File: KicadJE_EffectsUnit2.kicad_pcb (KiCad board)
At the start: 2 copper layers, 100 x 100 mm, 275 parts, among them J201 CV1, J202 CV2, J203 OUT1, J204 OUT2, J205 IN1, J206 IN2, J301 AVR-ISP-6, J302 UART, J401 CV1, J402 CV2, J403 OUT1, J404 OUT2, J405 OUT3, J406 OUT4, J407 IN1, J408 IN2, J409 I2C, J501 BOOT, J502 UART, J503 USB_B_Micro, J601 CV1, J602 FM_lin, J603 Sync, J604 PWM, J605 Ramp, J606 Tri, J608 555_Pulse, P201 Doepfer_Power_16pin, P401 Doepfer_Power_16pin, P601 Doepfer_Power_10pin, Q601 MMBT2222A, SW201 SW_SPDT, SW401 SW_SPDT, U201 TL072, U202 MCP4822, U301 ATmega32A-AU, U401 TL072, U402 TL072, U405 MCP4822, U501 AMS1117-3.3, U502 STM32F103C8Tx, U601 TLC555, U602 TL074, U603 TL074, Y301 16MHz, Y501 8 MHz

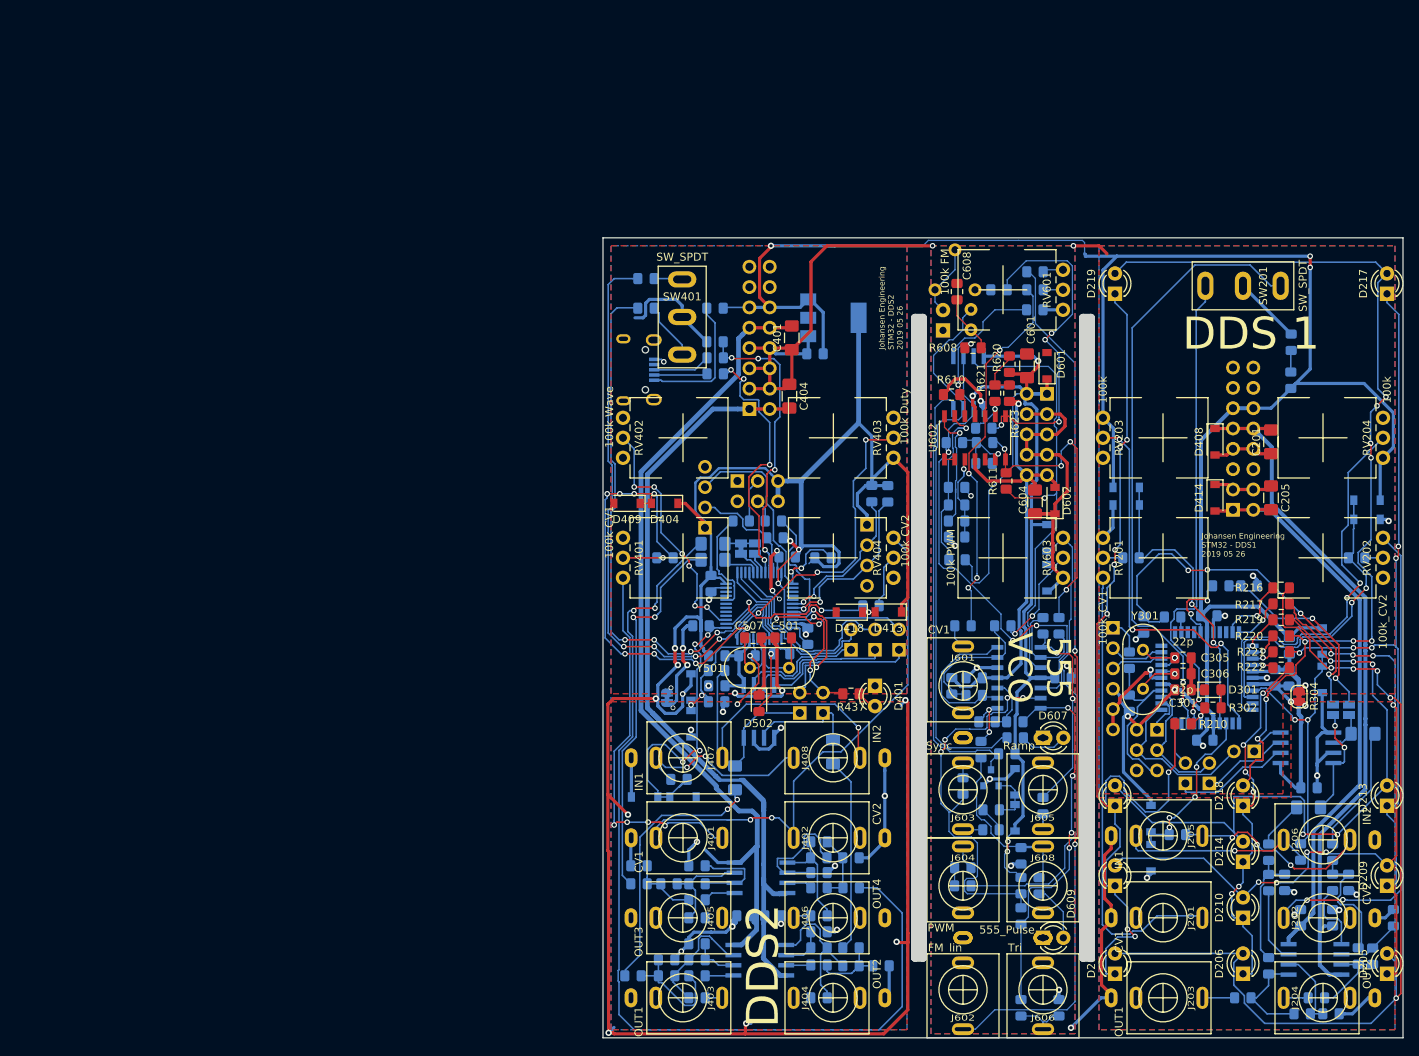
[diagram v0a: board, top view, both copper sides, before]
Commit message: New DPDT footprint
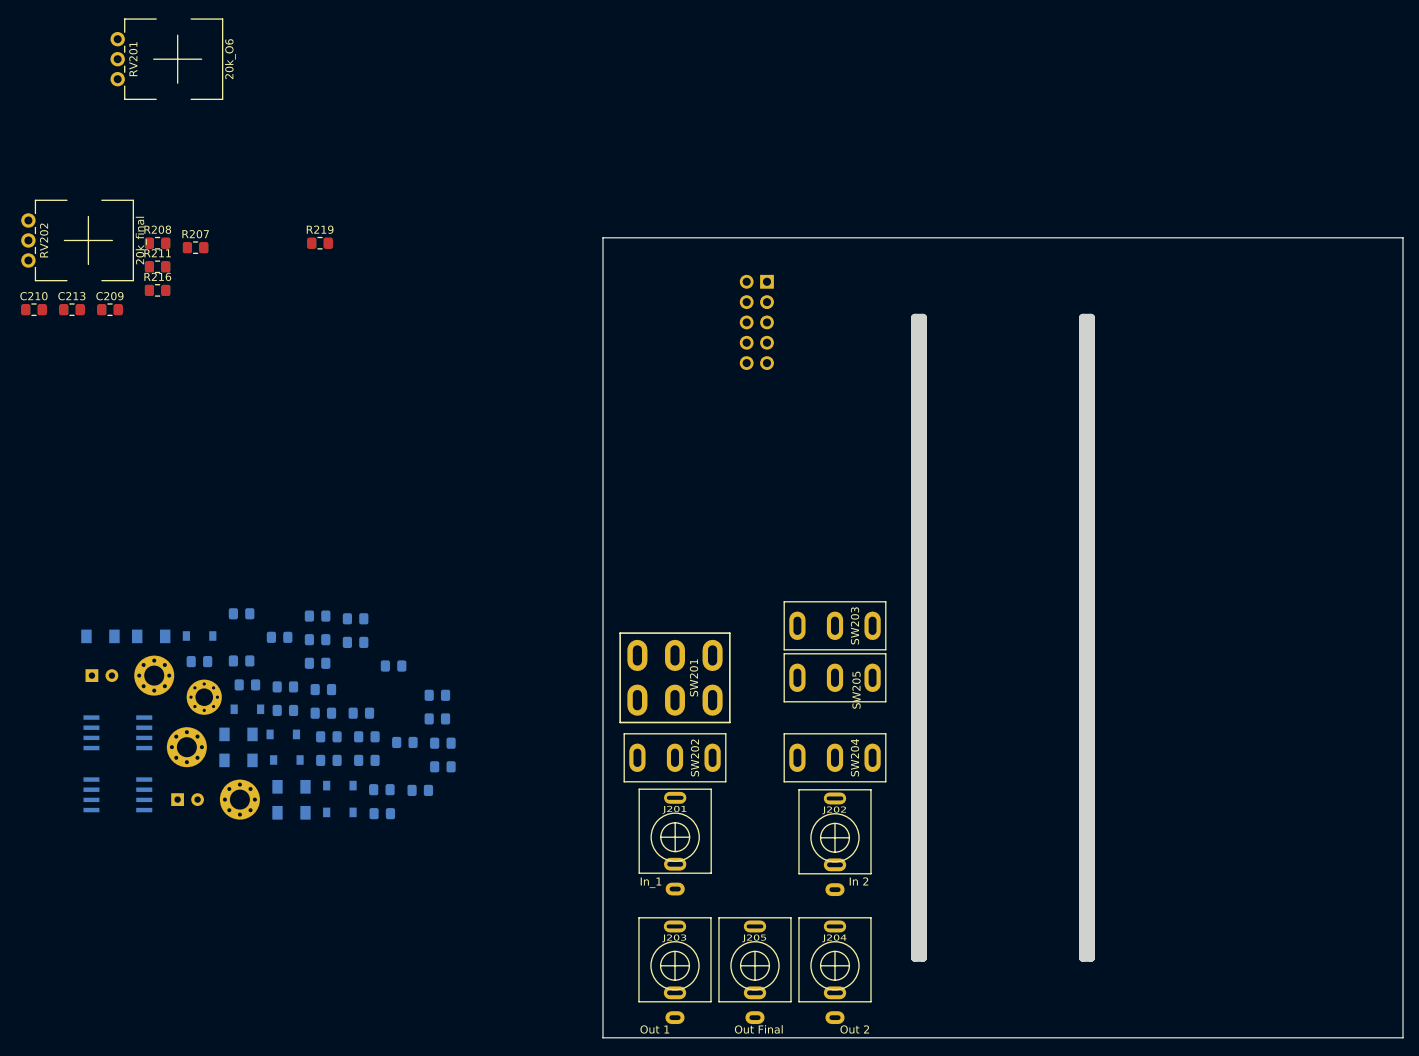
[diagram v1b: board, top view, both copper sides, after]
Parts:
- removed C301, C302, C303, C304, C307, C402, C403, C405, C406, C409, C410, C411, C412, C415, C416, C417, C503, C504, C505, C506, C602, C603, C605: 100n, Capacitor_SMD:C_0805_2012Metric_Pad1.15x1.40mm_HandSolder
- removed C305, C306: 22p, Capacitor_SMD:C_0805_2012Metric_Pad1.15x1.40mm_HandSolder
- removed C401, C404, C407, C408, C413, C414, C601, C604: 1u, Capacitor_SMD:C_1206_3216Metric_Pad1.42x1.75mm_HandSolder
- removed C501, C507: 20p, Capacitor_SMD:C_0805_2012Metric_Pad1.15x1.40mm_HandSolder
- removed C502: 470n, Capacitor_SMD:C_0805_2012Metric_Pad1.15x1.40mm_HandSolder
- removed C606, C610, C611: 1n, Capacitor_SMD:C_0805_2012Metric_Pad1.15x1.40mm_HandSolder
- removed C607: 22n, Capacitor_SMD:C_0805_2012Metric_Pad1.15x1.40mm_HandSolder
- removed C608: 10n, Capacitor_SMD:C_0805_2012Metric_Pad1.15x1.40mm_HandSolder
- removed C609: 220n, Capacitor_SMD:C_0805_2012Metric_Pad1.15x1.40mm_HandSolder
- removed D215, D217, D218, D219, D401, D607, D609: LED, LED_THT:LED_D3.0mm
- removed D216, D220, D404, D408, D409, D413, D414, D418, D419, D420, D421, D422, D601, D602, D603, D604, D605, D606: 1N1007, Diode_SMD:D_SOD-123
- removed D301, D501, D502: LED, LED_SMD:LED_0805_2012Metric_Pad1.15x1.40mm_HandSolder
- removed D611: Vactrol, LED_THT:LED_D3.0mm
- removed J206, J408: IN2, AJ-Dropbox-Kicad:PJ301SM
- removed J301: AVR-ISP-6, Connector_PinHeader_2.54mm:PinHeader_2x03_P2.54mm_Vertical
- removed J302: UART, Connector_PinHeader_2.54mm:PinHeader_1x06_P2.54mm_Vertical
- removed J401, J601: CV1, AJ-Dropbox-Kicad:PJ301SM
- removed J402: CV2, AJ-Dropbox-Kicad:PJ301SM
- removed J403: OUT1, AJ-Dropbox-Kicad:PJ301SM
- removed J404: OUT2, AJ-Dropbox-Kicad:PJ301SM
- removed J405: OUT3, AJ-Dropbox-Kicad:PJ301SM
- removed J406: OUT4, AJ-Dropbox-Kicad:PJ301SM
- removed J407: IN1, AJ-Dropbox-Kicad:PJ301SM
- removed J409: I2C, Connector_PinHeader_2.54mm:PinHeader_1x04_P2.54mm_Vertical
- removed J501: BOOT, Connector_PinHeader_2.54mm:PinHeader_2x03_P2.54mm_Vertical
- removed J502: UART, Connector_PinHeader_2.54mm:PinHeader_1x04_P2.54mm_Vertical
- removed J503: USB_B_Micro, Connector_USB:USB_Micro-B_Wuerth_629105150521
- removed J602: FM_lin, AJ-Dropbox-Kicad:PJ301SM
- removed J603: Sync, AJ-Dropbox-Kicad:PJ301SM
- removed J604: PWM, AJ-Dropbox-Kicad:PJ301SM
- removed J605: Ramp, AJ-Dropbox-Kicad:PJ301SM
- removed J606: Tri, AJ-Dropbox-Kicad:PJ301SM
- removed J608: 555_Pulse, AJ-Dropbox-Kicad:PJ301SM
- removed JP201: SS, Connector_PinSocket_2.54mm:PinSocket_1x02_P2.54mm_Vertical
- removed JP202: MOSI, Connector_PinSocket_2.54mm:PinSocket_1x02_P2.54mm_Vertical
- removed JP203: PWM1, Jumper:SolderJumper-2_P1.3mm_Open_Pad1.0x1.5mm
- removed JP204, JP404: SCK, Connector_PinSocket_2.54mm:PinSocket_1x02_P2.54mm_Vertical
- removed JP205: PWM2, Jumper:SolderJumper-2_P1.3mm_Open_Pad1.0x1.5mm
- removed JP401: PA9, Jumper:SolderJumper-2_P1.3mm_Bridged_Pad1.0x1.5mm
- removed JP402: PA10, Jumper:SolderJumper-2_P1.3mm_Open_Pad1.0x1.5mm
- removed JP403: CS, Connector_PinSocket_2.54mm:PinSocket_1x02_P2.54mm_Vertical
- removed JP405: SDI, Connector_PinSocket_2.54mm:PinSocket_1x02_P2.54mm_Vertical
- removed JP406: PWM1, Connector_PinSocket_2.54mm:PinSocket_1x02_P2.54mm_Vertical
- removed JP407: PWM2, Connector_PinSocket_2.54mm:PinSocket_1x02_P2.54mm_Vertical
- removed P401: Doepfer_Power_16pin, Connectors_IDC:IDC-Header_2x08_Pitch2.54mm_Straight
- removed P601: Doepfer_Power_10pin, Connectors_IDC:IDC-Header_2x05_Pitch2.54mm_Straight
- removed Q601: MMBT2222A, Package_TO_SOT_SMD:SOT-23
- removed R301, R504: 0R, Resistor_SMD:R_0805_2012Metric_Pad1.15x1.40mm_HandSolder
- removed R302, R615, R625: 1k, Resistor_SMD:R_0805_2012Metric_Pad1.15x1.40mm_HandSolder
- removed R303, R634: OPEN, Resistor_SMD:R_0805_2012Metric_Pad1.15x1.40mm_HandSolder
- removed R304, R505: 0R, Jumper:SolderJumper-2_P1.3mm_Bridged_RoundedPad1.0x1.5mm
- removed R305, R401, R402, R403, R404, R405, R406, R409, R410, R411, R412, R413, R414, R415, R416, R417, R418, R421, R422, R423, R424, R425, R426, R427, R428, R503, R506, R601, R611, R612, R613, R624, R626, R628: 10k, Resistor_SMD:R_0805_2012Metric_Pad1.15x1.40mm_HandSolder
- removed R407, R408, R419, R420: 100R, Resistor_SMD:R_0805_2012Metric_Pad1.15x1.40mm_HandSolder
- removed R435, R436, R509, R510, R605, R609, R637: 100k, Resistor_SMD:R_0805_2012Metric_Pad1.15x1.40mm_HandSolder
- removed R437: 820R, Resistor_SMD:R_0805_2012Metric_Pad1.15x1.40mm_HandSolder
- removed R501: 3k3, Resistor_SMD:R_0805_2012Metric_Pad1.15x1.40mm_HandSolder
- removed R502, R631: 2k2, Resistor_SMD:R_0805_2012Metric_Pad1.15x1.40mm_HandSolder
- removed R507, R511, R512: 10R, Resistor_SMD:R_0805_2012Metric_Pad1.15x1.40mm_HandSolder
- removed R508, R608: 1k5, Resistor_SMD:R_0805_2012Metric_Pad1.15x1.40mm_HandSolder
- removed R602: 12k, Resistor_SMD:R_0805_2012Metric_Pad1.15x1.40mm_HandSolder
- removed R603, R610, R616, R617, R618, R619: 47k, Resistor_SMD:R_0805_2012Metric_Pad1.15x1.40mm_HandSolder
- removed R604: 150k, Resistor_SMD:R_0805_2012Metric_Pad1.15x1.40mm_HandSolder
- removed R606: 100r, Resistor_SMD:R_0805_2012Metric_Pad1.15x1.40mm_HandSolder
- removed R607: LDR03, OptoDevice:R_LDR_4.9x4.2mm_P2.54mm_Vertical
- removed R614, R627: 20k, Resistor_SMD:R_0805_2012Metric_Pad1.15x1.40mm_HandSolder
- removed R620, R623: 62k, Resistor_SMD:R_0805_2012Metric_Pad1.15x1.40mm_HandSolder
- removed R621, R622: 100k_test, Resistor_SMD:R_0805_2012Metric_Pad1.15x1.40mm_HandSolder
- removed R629, R630: 2k, Resistor_SMD:R_0805_2012Metric_Pad1.15x1.40mm_HandSolder
- removed R632: 2M2, Resistor_SMD:R_0805_2012Metric_Pad1.15x1.40mm_HandSolder
- removed R633: 3k, Resistor_SMD:R_0805_2012Metric_Pad1.15x1.40mm_HandSolder
- removed R635: 120k, Resistor_SMD:R_0805_2012Metric_Pad1.15x1.40mm_HandSolder
- removed R636: 1k8, Resistor_SMD:R_0805_2012Metric_Pad1.15x1.40mm_HandSolder
- removed RV203, RV204: 100k, Potentiometer_THT:Potentiometer_China_RK09_Single_Vertical_AJ
- removed RV401: 100k CV1, Potentiometer_THT:Potentiometer_China_RK09_Single_Vertical_AJ
- removed RV402: 100k Wave, Potentiometer_THT:Potentiometer_China_RK09_Single_Vertical_AJ
- removed RV403: 100k Duty, Potentiometer_THT:Potentiometer_China_RK09_Single_Vertical_AJ
- removed RV404: 100k CV2, Potentiometer_THT:Potentiometer_China_RK09_Single_Vertical_AJ
- removed RV601: 100k FM, Potentiometer_THT:Potentiometer_China_RK09_Single_Vertical_AJ
- removed RV602: 5k, Potentiometer_THT:Potentiometer_Piher_PT-6-V_Vertical
- removed RV603: 100k PWM, Potentiometer_THT:Potentiometer_China_RK09_Single_Vertical_AJ
- removed SW401: SW_SPDT, AJ:SP1MS1
- removed U301: ATmega32A-AU, Package_QFP:TQFP-44_10x10mm_P0.8mm
- removed U401, U402: TL072, AJ:AJ_SO-8_5.3x6.2mm_P1.27mm
- removed U405: MCP4822, AJ:AJ_SO-8_5.3x6.2mm_P1.27mm
- removed U501: AMS1117-3.3, Package_TO_SOT_SMD:SOT-223-3_TabPin2
- removed U502: STM32F103C8Tx, Package_QFP:LQFP-48_7x7mm_P0.5mm
- removed U601: TLC555, AJ-Dropbox-Kicad:AJ_SO-8_5.3x6.2mm_P1.27mm
- removed U602, U603: TL074, Package_SO:SOIC-14_3.9x8.7mm_P1.27mm
- removed Y301: 16MHz, Crystal:Crystal_HC49-U_Vertical
- removed Y501: 8 MHz, Crystal:Crystal_HC49-U_Vertical
- added H201: 2,5mm, MountingHole:MountingHole_2.5mm_Pad_Via, B.Cu at (4.62, 120.2)
- added H202: 2,5mm, MountingHole:MountingHole_2.5mm_Pad_Via, B.Cu at (-2.01, 113.7)
- added H203: 2,2mm, MountingHole:MountingHole_2.5mm_Pad_Via, B.Cu at (-6.09, 104.7)
- added H204: 2,2mm, MountingHole:MountingHole_2.2mm_M2_Pad_Via, B.Cu at (0.16, 107.4)
- added SW202: In or cascade, AJ-Dropbox-Kicad:SP1MS1, F.Cu at (59.0, 115.0)
- added SW203: In or cascade, AJ-Dropbox-Kicad:SP1MS1, F.Cu at (79.0, 98.5)
- added SW204: In or cascade, AJ-Dropbox-Kicad:SP1MS1, F.Cu at (79.0, 115.0)
- added SW205: HI/LO, AJ-Dropbox-Kicad:SP1MS1, F.Cu at (79.0, 105.0)
- C201, C205: value 1u -> 100uF 16v; footprint Capacitor_SMD:C_1206_3216Metric_Pad1.42x1.75mm_HandSolder -> Capacitor_THT:CP_Radial_D5.0mm_P2.50mm; moved to B.Cu
- C204, C208: value 100n -> 1u
- C207: value 1u -> 100n; footprint Capacitor_SMD:C_1206_3216Metric_Pad1.42x1.75mm_HandSolder -> Capacitor_SMD:C_0805_2012Metric_Pad1.15x1.40mm_HandSolder
- C209, C213: moved to F.Cu
- C210: value 1u -> 100n; footprint Capacitor_SMD:C_1206_3216Metric_Pad1.42x1.75mm_HandSolder -> Capacitor_SMD:C_0805_2012Metric_Pad1.15x1.40mm_HandSolder; moved to F.Cu
- C212: value 100n -> 33n
- D205, D206: value LED -> 1N1007; footprint LED_THT:LED_D3.0mm -> Diode_SMD:D_SOD-123; moved to B.Cu
- D207, D209, D210, D211: value LED -> LL4148; footprint LED_THT:LED_D3.0mm -> Diode_SMD:D_MiniMELF; moved to B.Cu
- D208, D212: value 1N1007 -> LL4148; footprint Diode_SMD:D_SOD-123 -> Diode_SMD:D_MiniMELF
- D213: value LED -> LED_11dist; footprint LED_THT:LED_D3.0mm -> LED_SMD:LED_0805_2012Metric_Pad1.15x1.40mm_HandSolder; moved to B.Cu
- D214: value LED -> LED_11dist; footprint LED_THT:LED_D3.0mm -> Diode_SMD:D_0805_2012Metric_Pad1.15x1.40mm_HandSolder; moved to B.Cu
- J201: value CV1 -> In_1
- J202: value CV2 -> In 2
- J203: value OUT1 -> Out 1
- J204: value OUT2 -> Out 2
- J205: value IN1 -> Out Final
- P201: value Doepfer_Power_16pin -> Doepfer_Power_10pin; footprint Connectors_IDC:IDC-Header_2x08_Pitch2.54mm_Straight -> Connectors_IDC:IDC-Header_2x05_Pitch2.54mm_Straight
- R202, R204: value 10k -> OPEN
- R207: value 100R -> 10k; moved to F.Cu
- R208: value 10k -> 100k; moved to F.Cu
- R209, R214: value 10k -> 150R
- R210: value 100R -> 470R; moved to B.Cu
- R211: value 10k -> 1k; moved to F.Cu
- R213: value 100R -> 10k
- R216: value 100R -> 1k
- R217, R221, R222: value 100R -> 10k; moved to B.Cu
- R218: value 1k -> 4k7
- R219: value 100R -> 150R
- R220: value 100R -> 150R; moved to B.Cu
- R223: value 1k -> 100R
- RV201: value 100k_CV1 -> 20k_O6
- RV202: value 100k_CV2 -> 20k_final
- SW201: value SW_SPDT -> Dist 6; footprint AJ:SP1MS1 -> AJ-Dropbox-Kicad:SPDTx2
- U201: footprint AJ:AJ_SO-8_5.3x6.2mm_P1.27mm -> AJ-Dropbox-Kicad:AJ_SO-8_5.3x6.2mm_P1.27mm
- U202: value MCP4822 -> TL072; footprint AJ:AJ_SO-8_5.3x6.2mm_P1.27mm -> AJ-Dropbox-Kicad:AJ_SO-8_5.3x6.2mm_P1.27mm
- moved C209 175.7 mm to (-11.6, 59.0), turned to 0 degrees
- moved R211 174.6 mm to (-5.67, 53.6), turned to 0 degrees
- moved C210 174.4 mm to (-21.1, 59.0), turned to 0 degrees
- moved RV202 172.8 mm to (-21.8, 52.8), turned to 0 degrees
- moved R207 161.0 mm to (-0.92, 51.2), turned to 0 degrees
- moved R208 160.2 mm to (-5.67, 50.7), turned to 0 degrees
- moved D209 157.6 mm to (-6.47, 99.8), turned to 0 degrees
- moved U201 152.3 mm to (-10.6, 111.9)
- moved C213 151.1 mm to (-16.4, 59.0), turned to 0 degrees
- moved C201 150.3 mm to (-13.9, 104.7), turned to 0 degrees
- moved U202 148.8 mm to (-10.6, 119.6)
- moved D203 146.9 mm to (-0.42, 99.8), turned to 0 degrees
- moved D205 146.2 mm to (5.55, 108.9), turned to 0 degrees
- moved R216 145.3 mm to (-5.67, 56.6)
- moved D213 143.2 mm to (5.55, 105.9), turned to 0 degrees
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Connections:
- C201 pad 1: GND -> (no net)
- C201 pad 2: +12V -> Net-(C201-Pad2)
- C202 pad 1: GND -> Net-(C202-Pad1)
- C202 pad 2: +12V -> (no net)
- C203 pad 1: GND -> Net-(C203-Pad1)
- C203 pad 2: +5VA -> (no net)
- C204 pad 1: GND -> Net-(C204-Pad1)
- C204 pad 2: -12V -> In1
- C205 pad 1: GND -> Net-(C201-Pad2)
- C205 pad 2: -12V -> (no net)
- C206 pad 1: /KicadJE_ATMega32A_DAC/1_out -> (no net)
- C206 pad 2: Net-(C206-Pad2) -> Net-(C202-Pad1)
- C207 pad 1: Net-(C207-Pad1) -> (no net)
- C207 pad 2: DACA -> Net-(C203-Pad1)
- C208 pad 1: Net-(C206-Pad2) -> Net-(C208-Pad1)
- C208 pad 2: GND -> In2
- C209 pad 1: /KicadJE_ATMega32A_DAC/2_out -> Out1Dist
- C210 pad 2: DACB -> Out1Dist
- C211 pad 1: Net-(C209-Pad2) -> Out2Dist
- C211 pad 2: GND -> (no net)
- C212 pad 1: GND -> Net-(C212-Pad1)
- C212 pad 2: PWM12 -> GND
- C213 pad 1: GND -> Net-(C213-Pad1)
- C213 pad 2: PWM15 -> Net-(C213-Pad2)
- D201 pad 1: +5V -> (no net)
- D201 pad 2: CV1 -> Net-(D201-Pad2)
- D202 pad 1: CV1 -> Net-(D201-Pad2)
- D202 pad 2: GND -> (no net)
- D203 pad 1: +5V -> Net-(D203-Pad1)
- D203 pad 2: CV2 -> Net-(D203-Pad2)
- D204 pad 1: CV2 -> Net-(D203-Pad2)
- D204 pad 2: GND -> Net-(D203-Pad1)
- D205 pad 1: C0_22 -> GND
- D205 pad 2: R0_18 -> Net-(C210-Pad1)
- D206 pad 1: C1_23 -> Net-(C210-Pad1)
- D206 pad 2: R0_18 -> GND
- D207 pad 1: C2_0 -> Net-(D207-Pad1)
- D207 pad 2: R0_18 -> Net-(D207-Pad2)
- D208 pad 1: +5V -> Net-(D207-Pad2)
- D208 pad 2: IN1 -> Net-(D207-Pad1)
- D209 pad 1: C0_22 -> Net-(C213-Pad2)
- D209 pad 2: R1_19 -> GND
- D210 pad 1: C1_23 -> GND
- D210 pad 2: R1_19 -> Net-(C213-Pad2)
- D211 pad 1: C2_0 -> Net-(D211-Pad1)
- D211 pad 2: R1_19 -> Net-(D211-Pad2)
- D212 pad 1: IN1 -> Net-(D211-Pad2)
- D212 pad 2: GND -> Net-(D211-Pad1)
- D213 pad 1: C0_22 -> Net-(D213-Pad1)
- D213 pad 2: R2_20 -> OutFinal
- D214 pad 1: C1_23 -> OutFinal
- D214 pad 2: R2_20 -> Net-(D213-Pad1)
- J203 pad T: OUT1 -> Out1Dist
- J204 pad T: OUT2 -> Out2Dist
- J205 pad T: Net-(J205-PadT) -> OutFinal
- J205 pad TN: Net-(J205-PadTN) -> (no net)
- P201 pad 1: -12V -> +12V
- P201 pad 10: +12V -> -12V
- P201 pad 2: -12V -> +12V
- P201 pad 3: GND -> Net-(P201-Pad3)
- P201 pad 4: GND -> Net-(P201-Pad3)
- P201 pad 5: GND -> Net-(P201-Pad3)
- P201 pad 6: GND -> Net-(P201-Pad3)
- P201 pad 7: GND -> Net-(P201-Pad3)
- P201 pad 8: GND -> Net-(P201-Pad3)
- P201 pad 9: +12V -> -12V
- R201 pad 1: Net-(R201-Pad1) -> Net-(J201-PadT)
- R201 pad 2: CV1 -> Net-(C204-Pad1)
- R202 pad 1: Net-(R202-Pad1) -> Net-(C204-Pad1)
- R202 pad 2: CV2 -> GND
- R203 pad 1: Net-(J205-PadT) -> Net-(J201-PadTN)
- R203 pad 2: IN1 -> Net-(C208-Pad1)
- R204 pad 1: Net-(J205-PadTN) -> Net-(C208-Pad1)
- R204 pad 2: IN2 -> GND
- R205 pad 1: /KicadJE_ATMega32A_DAC/1_inv -> Net-(D203-Pad1)
- R205 pad 2: /KicadJE_ATMega32A_DAC/1_out -> GND
- R206 pad 1: GND -> Net-(R206-Pad1)
- R206 pad 2: /KicadJE_ATMega32A_DAC/1_inv -> Net-(D203-Pad1)
- R207 pad 1: /KicadJE_ATMega32A_DAC/1_out -> Out1Dist
- R207 pad 2: OUT1 -> Net-(R207-Pad2)
- R208 pad 1: Net-(C206-Pad2) -> Net-(R208-Pad1)
- R208 pad 2: /KicadJE_ATMega32A_DAC/1_noninv -> (no net)
- R209 pad 1: Net-(C207-Pad1) -> Out1Dist
- R209 pad 2: Net-(C206-Pad2) -> Net-(R209-Pad2)
- R210 pad 1: 32_0_LED -> Net-(R210-Pad1)
- R210 pad 2: C2_0 -> Net-(C210-Pad1)
- R211 pad 1: /KicadJE_ATMega32A_DAC/2_inv -> Out2Dist
- R211 pad 2: /KicadJE_ATMega32A_DAC/2_out -> Net-(R211-Pad2)
- R212 pad 1: GND -> Net-(R212-Pad1)
- R212 pad 2: /KicadJE_ATMega32A_DAC/2_inv -> GND
- R213 pad 1: /KicadJE_ATMega32A_DAC/2_out -> Out2Dist
- R213 pad 2: OUT2 -> Net-(R212-Pad1)
- R214 pad 1: Net-(C209-Pad2) -> Out2Dist
- R214 pad 2: /KicadJE_ATMega32A_DAC/2_noninv -> Net-(R214-Pad2)
- R215 pad 1: Net-(C210-Pad1) -> Net-(C212-Pad1)
- R215 pad 2: Net-(C209-Pad2) -> Net-(D207-Pad1)
- R216 pad 1: /KicadJE_ATMega32A_DAC/ATMega32A.sch/18 -> Net-(C213-Pad2)
- R216 pad 2: R0_18 -> Out2Dist
- R217 pad 1: /KicadJE_ATMega32A_DAC/ATMega32A.sch/19 -> Net-(D211-Pad2)
- R217 pad 2: R1_19 -> GND
- R218 pad 1: 32_12_PWM -> Net-(R218-Pad1)
- R218 pad 2: PWM12 -> Net-(D211-Pad2)
- R219 pad 1: /KicadJE_ATMega32A_DAC/ATMega32A.sch/20 -> Net-(D211-Pad1)
- R219 pad 2: R2_20 -> GND
- R220 pad 1: /KicadJE_ATMega32A_DAC/ATMega32A.sch/21 -> OutFinal
- R220 pad 2: R3_21 -> Net-(R220-Pad2)
- R221 pad 1: /KicadJE_ATMega32A_DAC/ATMega32A.sch/22 -> Net-(R221-Pad1)
- R221 pad 2: C0_22 -> Out1Dist
- R222 pad 1: /KicadJE_ATMega32A_DAC/ATMega32A.sch/23 -> Net-(R221-Pad1)
- R222 pad 2: C1_23 -> Out2Dist
- R223 pad 1: 32_15_PWM -> Net-(D213-Pad1)
- R223 pad 2: PWM15 -> GND
- RV201 pad 1: Net-(J201-PadT) -> Net-(R206-Pad1)
- RV201 pad 2: Net-(R201-Pad1) -> Out1Dist
- RV201 pad 3: GND -> Out1Dist
- RV202 pad 1: Net-(J201-PadTN) -> Net-(R218-Pad1)
- RV202 pad 2: Net-(R202-Pad1) -> Net-(R220-Pad2)
- RV202 pad 3: GND -> Net-(R220-Pad2)
- SW201 pad 1: 32_2_INT2 -> Net-(R207-Pad2)
- SW201 pad 2: GND -> (no net)
- SW201 pad 3: 32_1 -> Net-(C209-Pad2)
- U201 pad 1: /KicadJE_ATMega32A_DAC/1_out -> Net-(R214-Pad2)
- U201 pad 2: /KicadJE_ATMega32A_DAC/1_inv -> Net-(R212-Pad1)
- U201 pad 3: /KicadJE_ATMega32A_DAC/1_noninv -> Net-(C212-Pad1)
- U201 pad 4: -12V -> (no net)
- U201 pad 5: /KicadJE_ATMega32A_DAC/2_noninv -> Net-(R208-Pad1)
- U201 pad 6: /KicadJE_ATMega32A_DAC/2_inv -> Net-(D203-Pad1)
- U201 pad 7: /KicadJE_ATMega32A_DAC/2_out -> Net-(R209-Pad2)
- U201 pad 8: +12V -> (no net)
- U202 pad 1: +5VA -> Net-(R220-Pad2)
- U202 pad 2: /KicadJE_ATMega32A_DAC/SS -> Net-(D211-Pad2)
- U202 pad 3: /KicadJE_ATMega32A_DAC/SCK -> Net-(R221-Pad1)
- U202 pad 4: /KicadJE_ATMega32A_DAC/SDI -> (no net)
- U202 pad 5: GND -> (no net)
- U202 pad 6: DACB -> (no net)
- U202 pad 7: GND -> (no net)
- U202 pad 8: DACA -> (no net)
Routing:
- net GND: track 389.0 -> 0.00 mm, vias 52 -> 0
- net +3V3: track 328.7 -> 0.00 mm, vias 12 -> 0
- net +12V: track 328.5 -> 0.00 mm, vias 4 -> 0
- net +5V: track 275.7 -> 0.00 mm, vias 5 -> 0
- net -12V: track 251.0 -> 0.00 mm, vias 1 -> 0
- net Net-(C408-Pad1): track 121.2 -> 0.00 mm, vias 2 -> 0
- net C2_0: track 121.2 -> 0.00 mm, vias 8 -> 0
- net R3_21: track 117.7 -> 0.00 mm, vias 9 -> 0
- net R0_18: track 113.3 -> 0.00 mm, vias 5 -> 0
- net Net-(C609-Pad2): track 109.6 -> 0.00 mm, vias 2 -> 0
- net C0_22: track 104.2 -> 0.00 mm, vias 5 -> 0
- net R1_19: track 84.1 -> 0.00 mm, vias 8 -> 0
- net R2_20: track 80.2 -> 0.00 mm, vias 5 -> 0
- net 32_2_INT2: track 76.4 -> 0.00 mm, vias 2 -> 0
- net /KicadJE_STM32F0/STM32F103C8/STM32_PC15: track 75.7 -> 0.00 mm, vias 4 -> 0
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- removed copper zone on B.Cu, net +12V
- removed copper zone on B.Cu, net +3V3
- removed copper zone on B.Cu, net +5V
- removed copper zone on F.Cu, net GND
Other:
- board text removed: "+5V"
- board text removed: "555 VCO"
- board text removed: "DDS 1"
- board text removed: "DDS1"
- board text removed: "DDS2"
- board text removed: "GND"
- board text removed: "Johansen Engineering 555 VCO 2019 05 30"
- board text removed: "Johansen Engineering STM32 - DDS1 2019 05 26"
- board text removed: "Johansen Engineering STM32 - DDS2 2019 05 26"

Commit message: ERC
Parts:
- moved RV202 110.1 mm to (86.5, 72.5), turned to 180 degrees
- moved RV201 78.1 mm to (51.5, 77.5)
- moved SW203 8.50 mm to (79.0, 90.0)
- moved SW201 7.00 mm to (59.0, 98.0)
- moved SW205 6.50 mm to (79.0, 98.5)
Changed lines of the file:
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@@
   )
   (module AJ-Dropbox-Kicad:SPDTx2 (layer F.Cu)
-    (at 59 105 90)
+    (at 59 98 90)
     (fp_text reference SW201 (at 0 2.413 90) (layer F.SilkS)
       (effects (font (size 1 1) (thickness 0.15)))
@@
       (net 21 "Net-(R210-Pad1)"))
     (model ${KIPRJMOD}/Local.pretty/SPDT.step
+      (at (xyz 0 0 0))
+      (scale (xyz 1 1 1))
+      (rotate (xyz 0 0 0))
+    )
+    (model C:/Users/anders/Documents/KiCad/Lib/aj_packages3d/3D/Switch/SPDT.step
       (at (xyz 0 0 0))
       (scale (xyz 1 1 1))
@@
   )
   (module Potentiometer_THT:Potentiometer_China_RK09_Single_Vertical_AJ (layer F.Cu)
-    (at -10.664999 30.175001)
+    (at 51.5 77.5)
     (descr "Potentiometer, vertical, Alps RK09K Single, http://www.alps.com/prod/info/E/HTML/Potentiometer/RotaryPotentiometers/RK09K/RK09K_list.html")
     (tags "Potentiometer vertical Alps RK09K Single")
@@
   )
   (module Potentiometer_THT:Potentiometer_China_RK09_Single_Vertical_AJ (layer F.Cu)
-    (at -21.824999 52.835001)
+    (at 86.5 72.5 180)
     (descr "Potentiometer, vertical, Alps RK09K Single, http://www.alps.com/prod/info/E/HTML/Potentiometer/RotaryPotentiometers/RK09K/RK09K_list.html")
     (tags "Potentiometer vertical Alps RK09K Single")
-    (fp_text reference RV202 (at 2 -2.5 90) (layer F.SilkS)
-      (effects (font (size 1 1) (thickness 0.15)))
-    )
-    (fp_text value 20k_final (at 14 -2.5 90) (layer F.SilkS)
+    (fp_text reference RV202 (at 2 -2.5 270) (layer F.SilkS)
+      (effects (font (size 1 1) (thickness 0.15)))
+    )
+    (fp_text value 20k_final (at 14 -2.5 270) (layer F.SilkS)
       (effects (font (size 1 1) (thickness 0.15)))
     )
@@
     (fp_line (start 13.25 4.15) (end 13.25 -9.15) (layer F.CrtYd) (width 0.05))
     (fp_line (start 13.25 -9.15) (end -1.15 -9.15) (layer F.CrtYd) (width 0.05))
-    (fp_text user %R (at 2 -2.5 90) (layer F.Fab)
+    (fp_text user %R (at 2 -2.5 270) (layer F.Fab)
       (effects (font (size 1 1) (thickness 0.15)))
     )
     (fp_line (start 7.5 0.5) (end 7.5 -5.5) (layer F.SilkS) (width 0.15))
     (fp_line (start 4.5 -2.5) (end 10.5 -2.5) (layer F.SilkS) (width 0.15))
-    (pad 3 thru_hole circle (at 0 -5) (size 1.8 1.8) (drill 1) (layers *.Cu *.Mask)
+    (pad 3 thru_hole circle (at 0 -5 180) (size 1.8 1.8) (drill 1) (layers *.Cu *.Mask)
       (net 39 "Net-(R220-Pad2)"))
-    (pad 2 thru_hole circle (at 0 -2.5) (size 1.8 1.8) (drill 1) (layers *.Cu *.Mask)
+    (pad 2 thru_hole circle (at 0 -2.5 180) (size 1.8 1.8) (drill 1) (layers *.Cu *.Mask)
       (net 39 "Net-(R220-Pad2)"))
-    (pad 1 thru_hole circle (at 0 0) (size 1.8 1.8) (drill 1) (layers *.Cu *.Mask)
+    (pad 1 thru_hole circle (at 0 0 180) (size 1.8 1.8) (drill 1) (layers *.Cu *.Mask)
       (net 38 "Net-(R218-Pad1)"))
-    (pad "" np_thru_hole oval (at 7 -6.9) (size 4 3) (drill oval 3 2) (layers *.Cu *.Mask))
-    (pad "" np_thru_hole oval (at 7 1.9) (size 4 3) (drill oval 3 2) (layers *.Cu *.Mask))
+    (pad "" np_thru_hole oval (at 7 -6.9 180) (size 4 3) (drill oval 3 2) (layers *.Cu *.Mask))
+    (pad "" np_thru_hole oval (at 7 1.9 180) (size 4 3) (drill oval 3 2) (layers *.Cu *.Mask))
     (model ${KISYS3DMOD}/Potentiometer_THT.3dshapes/Potentiometer_Alps_RK09K_Single_Vertical.wrl
       (at (xyz 0 0 0))
@@
       (rotate (xyz 0 0 0))
     )
+    (model C:/Users/anders/Documents/KiCad/Lib/aj_packages3d/3D/Switch/SPDT.step
+      (at (xyz 0 0 0))
+      (scale (xyz 1 1 1))
+      (rotate (xyz 0 0 0))
+    )
   )
   (module AJ-Dropbox-Kicad:SP1MS1 (layer F.Cu)
-    (at 79 98.5 90)
+    (at 79 90 90)
     (fp_text reference SW203 (at 0 2.54 90) (layer F.SilkS)
       (effects (font (size 1 1) (thickness 0.15)))
@@
       (net 36 "Net-(R211-Pad2)"))
     (model ${KIPRJMOD}/Local.pretty/SPDT.step
+      (at (xyz 0 0 0))
+      (scale (xyz 1 1 1))
+      (rotate (xyz 0 0 0))
+    )
+    (model C:/Users/anders/Documents/KiCad/Lib/aj_packages3d/3D/Switch/SPDT.step
       (at (xyz 0 0 0))
       (scale (xyz 1 1 1))
@@
       (rotate (xyz 0 0 0))
     )
+    (model C:/Users/anders/Documents/KiCad/Lib/aj_packages3d/3D/Switch/SPDT.step
+      (at (xyz 0 0 0))
+      (scale (xyz 1 1 1))
+      (rotate (xyz 0 0 0))
+    )
   )
   (module AJ-Dropbox-Kicad:SP1MS1 (layer F.Cu)
-    (at 79 105 90)
+    (at 79 98.5 90)
     (fp_text reference SW205 (at -1.535001 2.724999 90) (layer F.SilkS)
       (effects (font (size 1 1) (thickness 0.15)))
@@
       (at (xyz 0 0 0))
       (scale (xyz 1 1 1))
+      (rotate (xyz 0 0 0))
+    )
+    (model C:/Users/anders/Documents/KiCad/Lib/aj_packages3d/3D/Switch/SPDT.step
+      (at (xyz 0 0 0))
+      (scale (xyz 1 1 1))
